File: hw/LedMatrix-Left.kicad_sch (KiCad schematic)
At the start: 78 parts, among them Q3200 DTA114E, Q3201 DTA114E, Q3202 DTA114E, Q3203 DTA114E, Q3204 DTA114E, Q3205 DTA114E, Q3206 DTA114E, Q3207 DTA114E, Q3208 DTA114E, Q3209 DTA114E, Q3210 DTC114EE, Q3211 DTC114EE, Q3212 DTC114EE, Q3213 DTC114EE, Q3214 DTC114EE, Q3215 DTC114EE, Q3216 DTC114EE, Q3217 DTC114EE, Q3218 DTC114EE, Q3219 DTC114EE, Q3220 DTC114EE, Q3221 DTC114EE, X3200 Lightpipe-5x5mm-Dome, X3201 Lightpipe-5x5mm-Dome, X3202 Lightpipe-5x5mm-Dome, X3203 Lightpipe-5x5mm-Dome

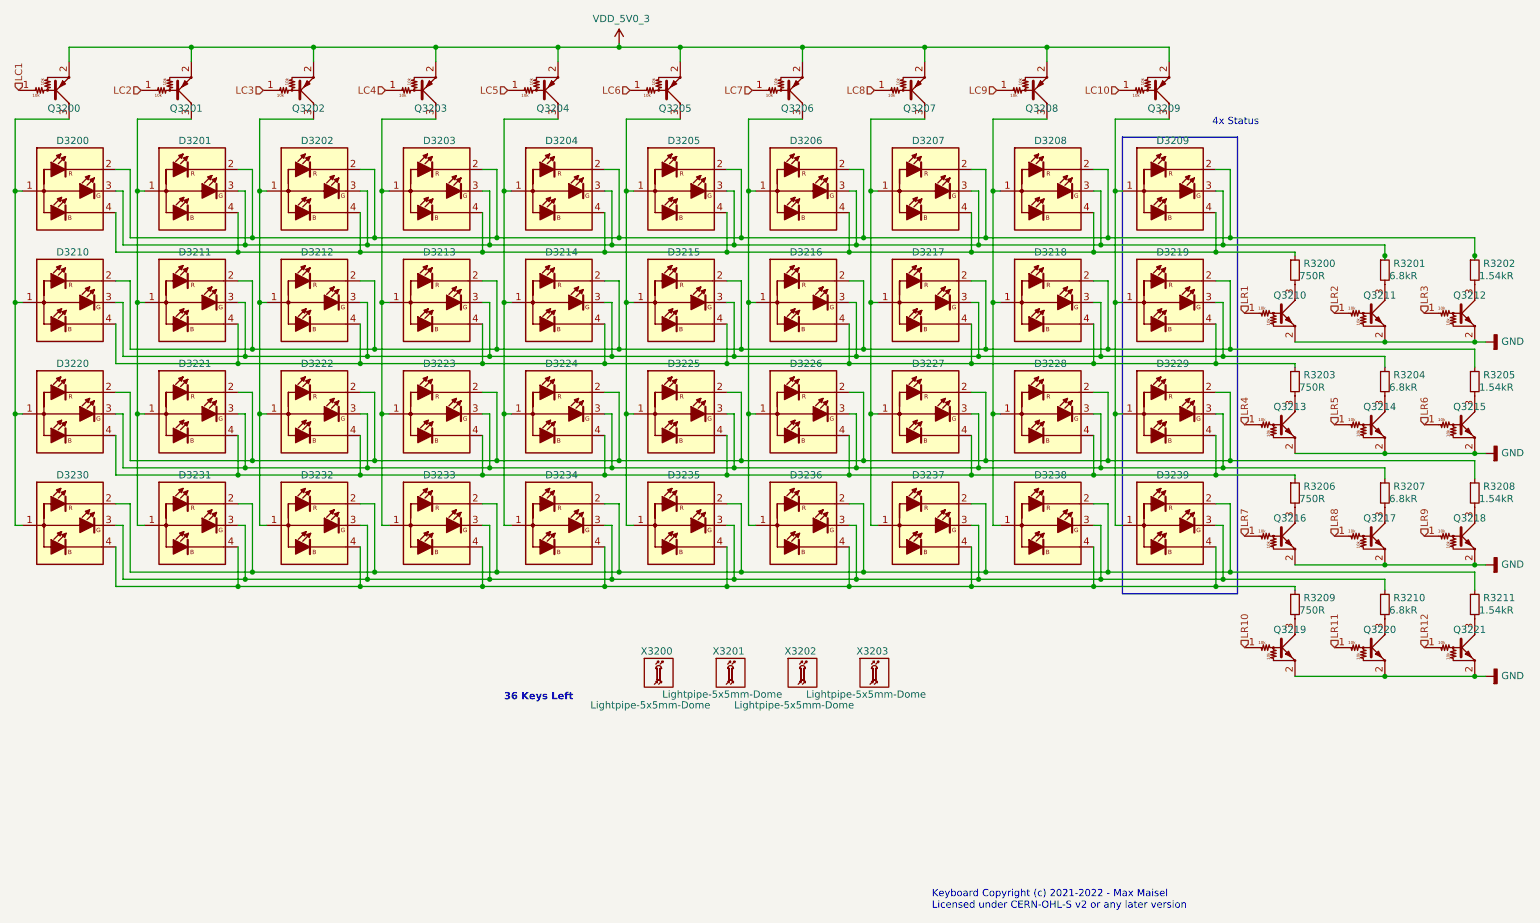
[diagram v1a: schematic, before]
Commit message: Update schematic:
- Add ESD protection.
- Adjust distance bolts so they fit to the MX mounting plate.
- Make key layout symmetric.
- Add resistor to TX driver outputs.
- Use alternate IO functions on inter-board connectors.
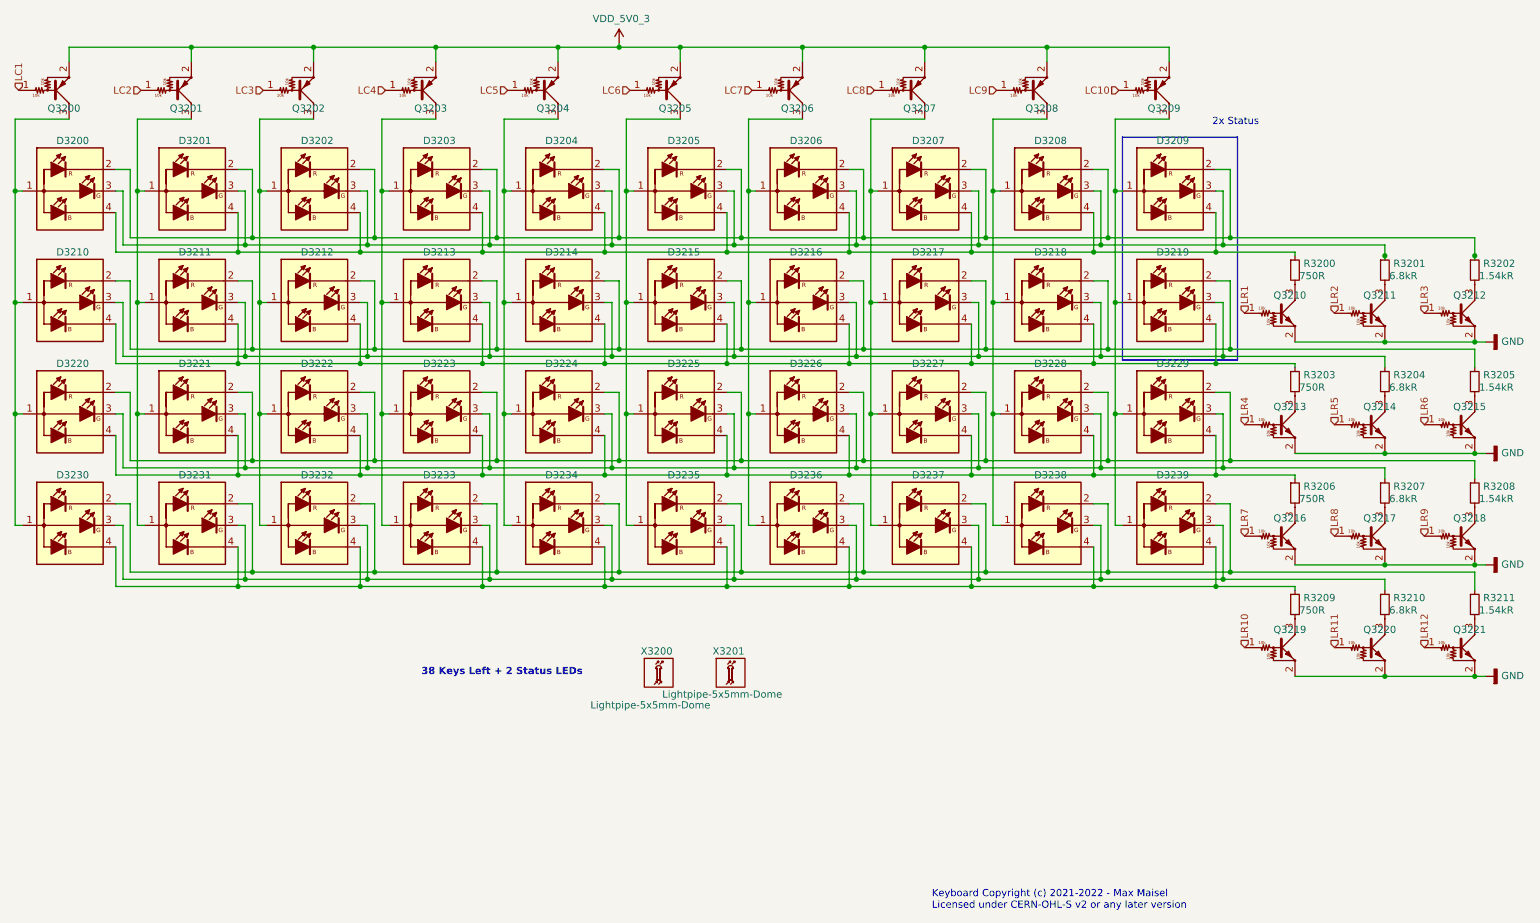
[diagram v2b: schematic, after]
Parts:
- removed X3202, X3203: Lightpipe-5x5mm-Dome, Keyboard:Lightpipe-51513530188F, symbol Keyboard:Lightpipe-5x5mm-Dome
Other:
- note added: "2x Status"
- note added: "38 Keys Left + 2 Status LEDs"
- note removed: "36 Keys Left"
- note removed: "4x Status"
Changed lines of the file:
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@@
     (stroke (width 0) (type default) (color 0 0 0 0))
   )
-  (polyline (pts (xy 231.775 115.57) (xy 211.455 115.57))
+  (polyline (pts (xy 231.775 74.295) (xy 211.455 74.295))
     (stroke (width 0) (type default) (color 0 0 0 0))
   )
@@
     (stroke (width 0) (type default) (color 0 0 0 0))
   )
-  (polyline (pts (xy 211.455 115.57) (xy 211.455 34.925))
+  (polyline (pts (xy 211.455 74.295) (xy 211.455 34.925))
     (stroke (width 0) (type default) (color 0 0 0 0))
   )
@@
     (stroke (width 0) (type default) (color 0 0 0 0))
   )
-  (polyline (pts (xy 231.775 34.925) (xy 231.775 115.57))
+  (polyline (pts (xy 231.775 34.925) (xy 231.775 74.295))
     (stroke (width 0) (type default) (color 0 0 0 0))
   )
@@
     (stroke (width 0) (type default) (color 0 0 0 0))
   )
-  (text "36 Keys Left" (at 102.235 134.62 0)
+  (text "38 Keys Left + 2 Status LEDs" (at 87.63 130.175 0)
     (effects (font (size 1.27 1.27) (thickness 0.254) bold) (justify left bottom))
   )
-  (text "4x Status" (at 227.33 33.02 0)
+  (text "2x Status" (at 227.33 33.02 0)
     (effects (font (size 1.27 1.27)) (justify left bottom))
   )
@@
     )
   )
-  (symbol (lib_id "Keyboard:Lightpipe-5x5mm-Dome") (at 154.94 129.54 0) (unit 1)
-    (in_bom yes) (on_board yes)
-    (property "Reference" "X3202" (id 0) (at 151.765 125.73 0)
-      (effects (font (size 1.27 1.27)) (justify left))
-    )
-    (property "Value" "Lightpipe-5x5mm-Dome" (id 1) (at 142.875 135.255 0)
-      (effects (font (size 1.27 1.27)) (justify left))
-    )
-    (property "Footprint" "Keyboard:Lightpipe-51513530188F" (id 2) (at 154.94 129.286 0)
-      (effects (font (size 1.27 1.27)) hide)
-    )
-    (property "Datasheet" "https://www.mouser.de/datasheet/2/109/Dialight_12192017_Panel%20Mount%205mm%20Lightpipe-1272673.pdf" (id 3) (at 154.94 129.286 0)
-      (effects (font (size 1.27 1.27)) hide)
-    )
-    (property "mouser#" "645-51513530188F" (id 4) (at 155.448 135.128 0)
-      (effects (font (size 1.27 1.27)) hide)
-    )
-    (property "manf#" "51513530188F" (id 5) (at 155.448 135.128 0)
-      (effects (font (size 1.27 1.27)) hide)
-    )
-  )
   (symbol (lib_id "Keyboard:Lightpipe-5x5mm-Dome") (at 142.24 129.54 0) (unit 1)
     (in_bom yes) (on_board yes)
@@
       (effects (font (size 1.27 1.27)) hide)
     )
-  )
-  (symbol (lib_id "Keyboard:Lightpipe-5x5mm-Dome") (at 167.64 129.54 0) (unit 1)
-    (in_bom yes) (on_board yes)
-    (property "Reference" "X3203" (id 0) (at 164.465 125.73 0)
-      (effects (font (size 1.27 1.27)) (justify left))
-    )
-    (property "Value" "Lightpipe-5x5mm-Dome" (id 1) (at 155.575 133.35 0)
-      (effects (font (size 1.27 1.27)) (justify left))
-    )
-    (property "Footprint" "Keyboard:Lightpipe-51513530188F" (id 2) (at 167.64 129.286 0)
-      (effects (font (size 1.27 1.27)) hide)
-    )
-    (property "Datasheet" "https://www.mouser.de/datasheet/2/109/Dialight_12192017_Panel%20Mount%205mm%20Lightpipe-1272673.pdf" (id 3) (at 167.64 129.286 0)
-      (effects (font (size 1.27 1.27)) hide)
-    )
-    (property "mouser#" "645-51513530188F" (id 4) (at 168.148 135.128 0)
-      (effects (font (size 1.27 1.27)) hide)
-    )
-    (property "manf#" "51513530188F" (id 5) (at 168.148 135.128 0)
-      (effects (font (size 1.27 1.27)) hide)
-    )

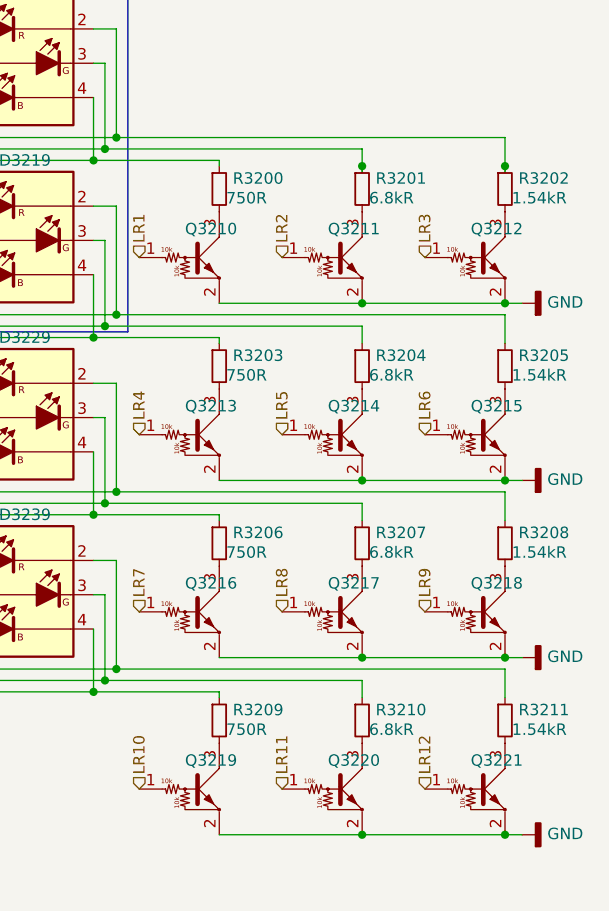
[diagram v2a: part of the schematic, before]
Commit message: Adjust LED matrix resistors.
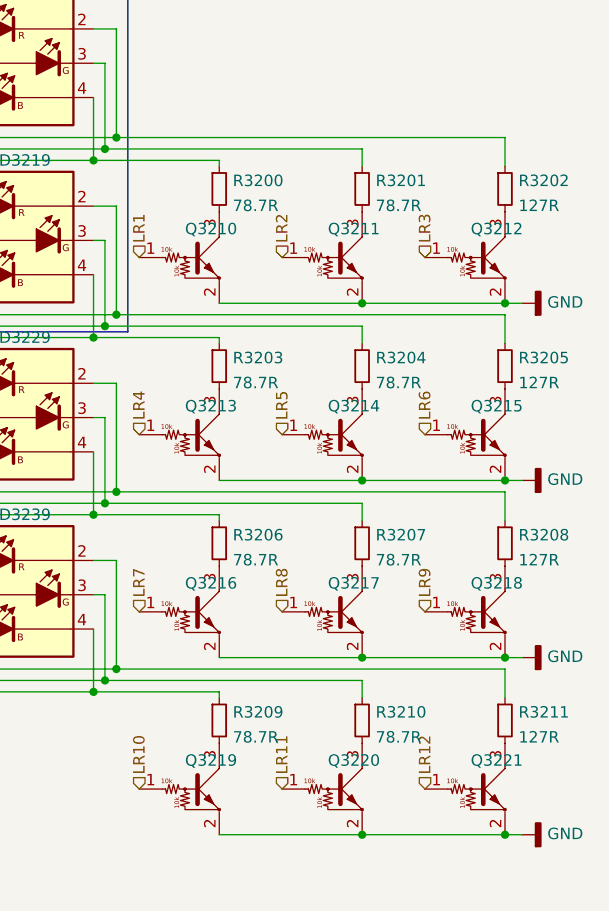
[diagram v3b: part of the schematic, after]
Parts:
- removed R3200, R3203, R3206, R3209: 750R, Keyboard:R_0402, symbol Keyboard:750R
- removed R3201, R3204, R3207, R3210: 6.8kR, Keyboard:R_0402, symbol Keyboard:6.8kR
- removed R3202, R3205, R3208, R3211: 1.54kR, Keyboard:R_0402, symbol Keyboard:1.54kR
- added R3200, R3201, R3203, R3204, R3206, R3207, R3209, R3210: 78.7R, Keyboard:R_0402, symbol Keyboard:78.7R
- added R3202, R3205, R3208, R3211: 127R, Keyboard:R_0402, symbol Keyboard:127R
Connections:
- net at D3220.2 (KR), D3221.2 (KR), D3222.2 (KR)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: now also R3208.1
- net at D3220.3 (KG), D3221.3 (KG), D3222.3 (KG)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: now also R3207.1
- net at D3220.4 (KB), D3221.4 (KB), D3222.4 (KB)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: now also R3206.1
- net at D3230.2 (KR), D3231.2 (KR), D3232.2 (KR)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: now also R3211.1
- net at D3230.3 (KG), D3231.3 (KG), D3232.3 (KG)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: now also R3210.1
- net at D3230.4 (KB), D3231.4 (KB), D3232.4 (KB)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: now also R3209.1
- net at Q3212.3 (C): now also R3202.2
- net at Q3211.3 (C): now also R3201.2
- net at D3200.2 (KR), D3201.2 (KR), D3202.2 (KR)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: now also R3202.1
- net at D3200.3 (KG), D3201.3 (KG), D3202.3 (KG)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: now also R3201.1
- net at D3200.4 (KB), D3201.4 (KB), D3202.4 (KB)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: now also R3200.1
- net at D3210.2 (KR), D3211.2 (KR), D3212.2 (KR)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: now also R3205.1
- net at D3210.3 (KG), D3211.3 (KG), D3212.3 (KG)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: now also R3204.1
- net at D3210.4 (KB), D3211.4 (KB), D3212.4 (KB)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: now also R3203.1
- net at Q3213.3 (C): now also R3203.2
- net at Q3214.3 (C): now also R3204.2
- net at Q3215.3 (C): now also R3205.2
- net at Q3216.3 (C): now also R3206.2
- net at Q3210.3 (C): now also R3200.2
- net at Q3218.3 (C): now also R3208.2
- net at Q3217.3 (C): now also R3207.2
- net at Q3220.3 (C): now also R3210.2
- net at Q3221.3 (C): now also R3211.2
- net at Q3219.3 (C): now also R3209.2
